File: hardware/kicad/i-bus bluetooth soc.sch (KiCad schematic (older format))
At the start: 25 parts, among them J1 CONN_3, J2 CONN_6, U1 MCP2025, U2 CC2541, X1 32 MHz

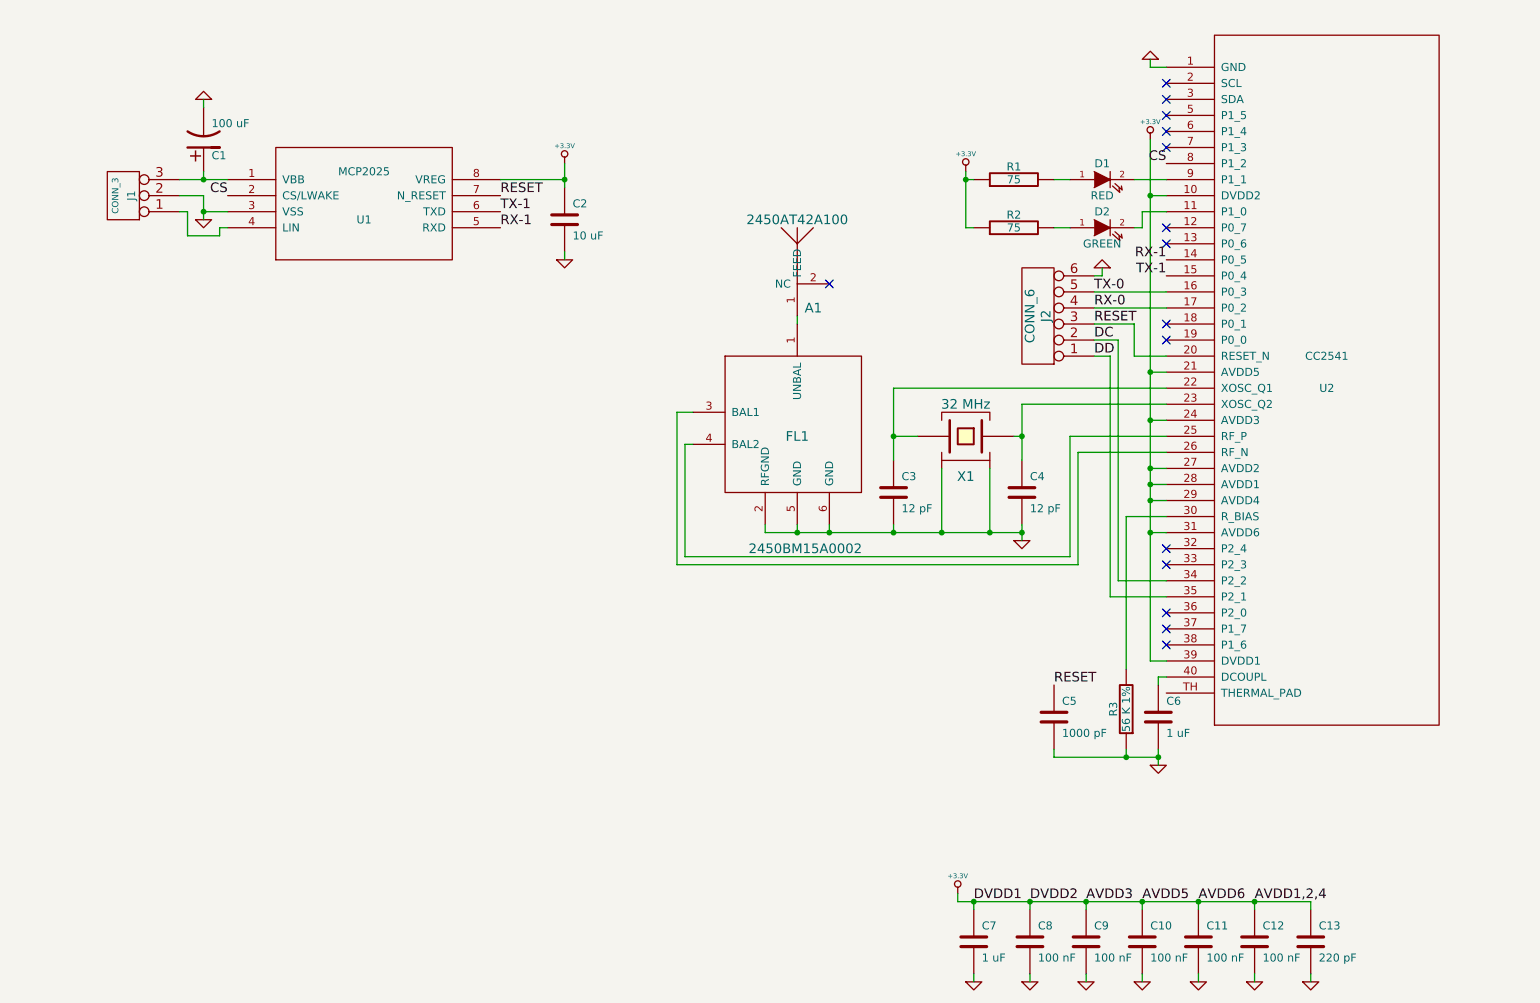
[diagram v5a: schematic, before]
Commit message: Connect thermal pad to ground
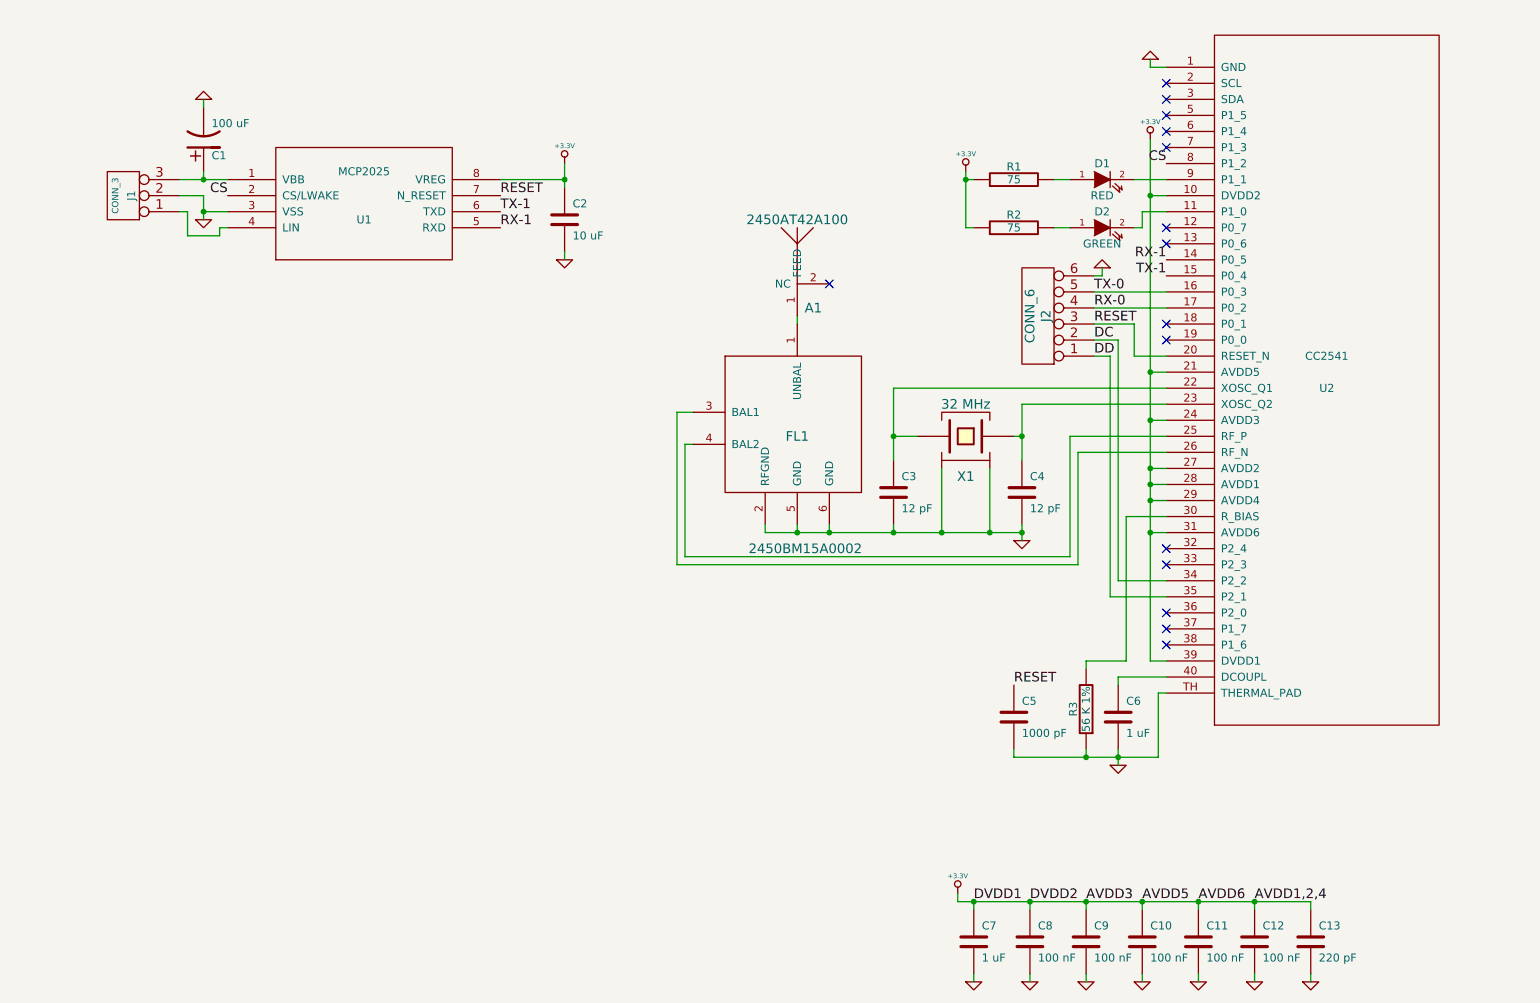
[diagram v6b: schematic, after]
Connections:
- net GND: now also U2.TH (THERMAL_PAD)
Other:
- moved on the sheet: C5, C6, R3
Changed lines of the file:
@@
 Connection ~ 2250 1800
 Wire Wire Line
-	2250 1850 2250 1700
+	2250 1700 2250 1850
 Wire Wire Line
 	2250 1700 2100 1700
@@
 	7750 6100 7750 6150
 Wire Wire Line
-	9150 6150 9150 6100
+	9150 6100 9150 6150
 Wire Wire Line
 	7400 6100 7400 6150
@@
 Wire Wire Line
 	8800 6550 8800 6600
-Connection ~ 8000 5200
-Wire Wire Line
-	8200 5200 7550 5200
-Wire Wire Line
-	7550 5200 7550 5150
+Connection ~ 7750 5200
+Wire Wire Line
+	7300 5200 8200 5200
+Wire Wire Line
+	7300 5200 7300 5150
 Wire Wire Line
 	7550 1600 7650 1600
@@
 Wire Wire Line
 	7650 3200 8250 3200
-Connection ~ 8200 5200
-Wire Wire Line
-	8000 5150 8000 5200
+Connection ~ 7950 5200
+Wire Wire Line
+	7750 5150 7750 5200
 Wire Wire Line
 	6550 3800 6550 3750
@@
 	6700 3200 6550 3200
 Wire Wire Line
-	7350 3350 7350 3000
-Wire Wire Line
-	8200 4750 8200 4700
-Wire Wire Line
-	8200 4700 8250 4700
-Wire Wire Line
-	8250 4600 8150 4600
+	7350 3000 7350 3350
+Wire Wire Line
+	7950 4750 7950 4700
+Wire Wire Line
+	7950 4700 8250 4700
+Wire Wire Line
+	8150 4600 8250 4600
 Connection ~ 8150 3600
 Wire Wire Line
@@
 Connection ~ 8150 3500
 Wire Wire Line
-	8250 3800 8150 3800
+	8150 3800 8250 3800
 Connection ~ 8150 3800
 Wire Wire Line
-	8150 4600 8150 1350
+	8150 1350 8150 4600
 Connection ~ 8150 1700
 Wire Wire Line
 	8250 900  8150 900
 Wire Wire Line
-	8200 5150 8200 5250
+	7950 5150 7950 5250
 Wire Wire Line
 	7350 3000 8250 3000
@@
 Connection ~ 7350 3200
 Wire Wire Line
-	7350 3850 7350 3750
+	7350 3750 7350 3850
 Connection ~ 7350 3800
 Wire Wire Line
 	8250 3700 8000 3700
 Wire Wire Line
-	8000 3700 8000 4650
+	8000 3700 8000 4600
 Wire Wire Line
 	8250 3300 7700 3300
@@
 Connection ~ 6550 3800
 Wire Wire Line
-	7350 3800 5750 3800
+	5750 3800 7350 3800
 Wire Wire Line
 	5750 3800 5750 3750
@@
 	1    0    0    -1
 $EndComp
-Text Label 7550 4750 0    60   ~ 0
+Text Label 7300 4750 0    60   ~ 0
 RESET
 $Comp
 L C C5
 U 1 1 53025324
-P 7550 4950
-F 0 "C5" H 7600 5050 50  0000 L CNN
-F 1 "1000 pF" H 7600 4850 50  0000 L CNN
-F 2 "" H 7550 4950 60  0001 C CNN
-F 3 "" H 7550 4950 60  0001 C CNN
-	1    7550 4950
+P 7300 4950
+F 0 "C5" H 7350 5050 50  0000 L CNN
+F 1 "1000 pF" H 7350 4850 50  0000 L CNN
+F 2 "" H 7300 4950 60  0001 C CNN
+F 3 "" H 7300 4950 60  0001 C CNN
+	1    7300 4950
 	1    0    0    -1
 $EndComp
@@
 L R R3
 U 1 1 5301993D
-P 8000 4900
-F 0 "R3" V 8080 4900 50  0000 C CNN
-F 1 "56 K 1%" V 8000 4900 50  0000 C CNN
-F 2 "" H 8000 4900 60  0001 C CNN
-F 3 "" H 8000 4900 60  0001 C CNN
-	1    8000 4900
+P 7750 4900
+F 0 "R3" V 7830 4900 50  0000 C CNN
+F 1 "56 K 1%" V 7750 4900 50  0000 C CNN
+F 2 "" H 7750 4900 60  0001 C CNN
+F 3 "" H 7750 4900 60  0001 C CNN
+	1    7750 4900
 	-1   0    0    1
 $EndComp
@@
 L GND #GND015
 U 1 1 5301988F
-P 8200 5250
-F 0 "#GND015" H 8200 5250 30  0001 C CNN
-F 1 "GND" H 8200 5180 30  0001 C CNN
-F 2 "" H 8200 5250 60  0001 C CNN
-F 3 "" H 8200 5250 60  0001 C CNN
-	1    8200 5250
+P 7950 5250
+F 0 "#GND015" H 7950 5250 30  0001 C CNN
+F 1 "GND" H 7950 5180 30  0001 C CNN
+F 2 "" H 7950 5250 60  0001 C CNN
+F 3 "" H 7950 5250 60  0001 C CNN
+	1    7950 5250
 	1    0    0    -1
 $EndComp
@@
 L C C6
 U 1 1 5301987F
-P 8200 4950
-F 0 "C6" H 8250 5050 50  0000 L CNN
-F 1 "1 uF" H 8250 4850 50  0000 L CNN
-F 2 "" H 8200 4950 60  0001 C CNN
-F 3 "" H 8200 4950 60  0001 C CNN
-	1    8200 4950
+P 7950 4950
+F 0 "C6" H 8000 5050 50  0000 L CNN
+F 1 "1 uF" H 8000 4850 50  0000 L CNN
+F 2 "" H 7950 4950 60  0001 C CNN
+F 3 "" H 7950 4950 60  0001 C CNN
+	1    7950 4950
 	1    0    0    -1
 $EndComp
@@
 	7000 1550 7000 1900
 Connection ~ 7000 1600
+Wire Wire Line
+	8000 4600 7750 4600
+Wire Wire Line
+	7750 4600 7750 4650
+Wire Wire Line
+	8250 4800 8200 4800
+Wire Wire Line
+	8200 4800 8200 5200
 $EndSCHEMATC
